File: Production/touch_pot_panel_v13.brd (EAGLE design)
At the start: 283 x 171.7 mm, 927 parts, among them U1 PIC16F1829, U10 5V, U11 PIC16F1829, U12 AD5262, U13 5V, U14 PIC16F1829, U15 AD5262, U16 5V, U17 PIC16F1829, U18 AD5262, U19 5V, U2 AD5262, U20 PIC16F1829, U21 AD5262, U22 5V, U23 PIC16F1829, U24 AD5262, U25 5V, U26 PIC16F1829, U27 AD5262, U28 5V, U29 PIC16F1829, U3 5V, U30 AD5262, U31 5V, U32 PIC16F1829, U33 AD5262, U34 5V, U35 PIC16F1829, U36 AD5262, U4 5V, U5 PIC16F1829, U6 AD5262, U7 5V, U8 PIC16F1829, U9 AD5262

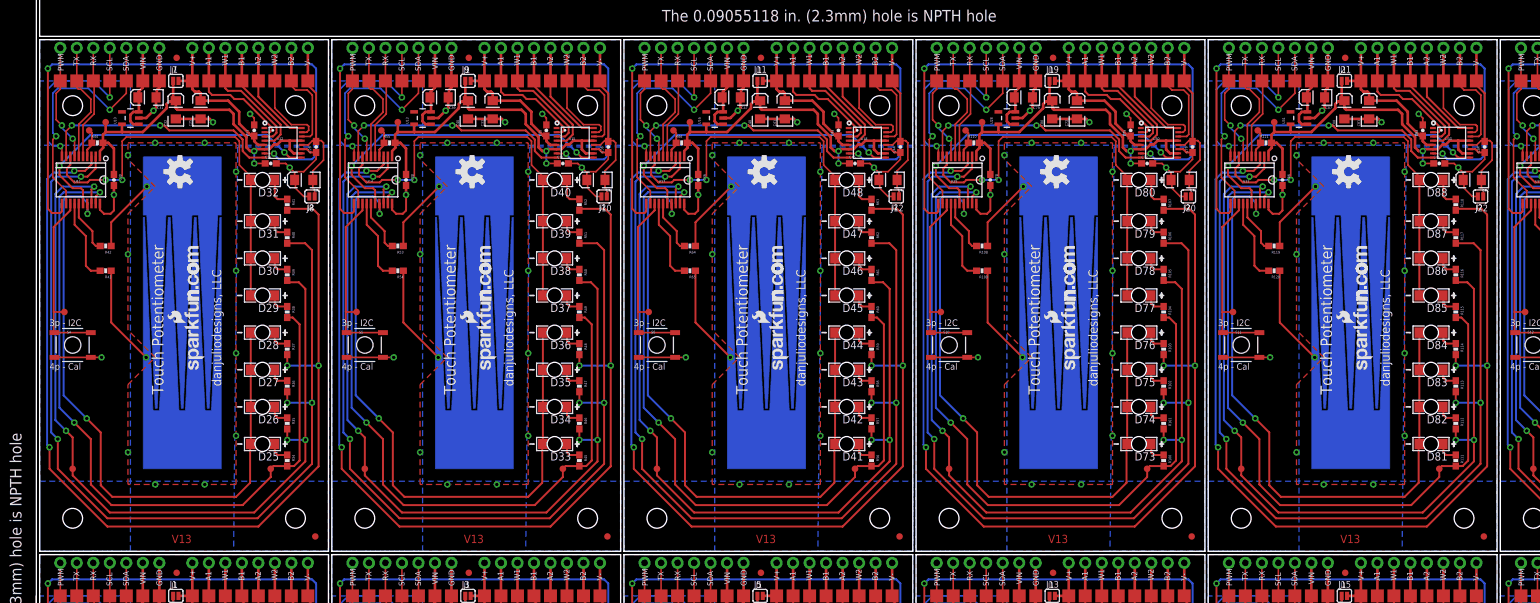
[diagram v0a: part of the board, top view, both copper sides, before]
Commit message: removed odd ground line
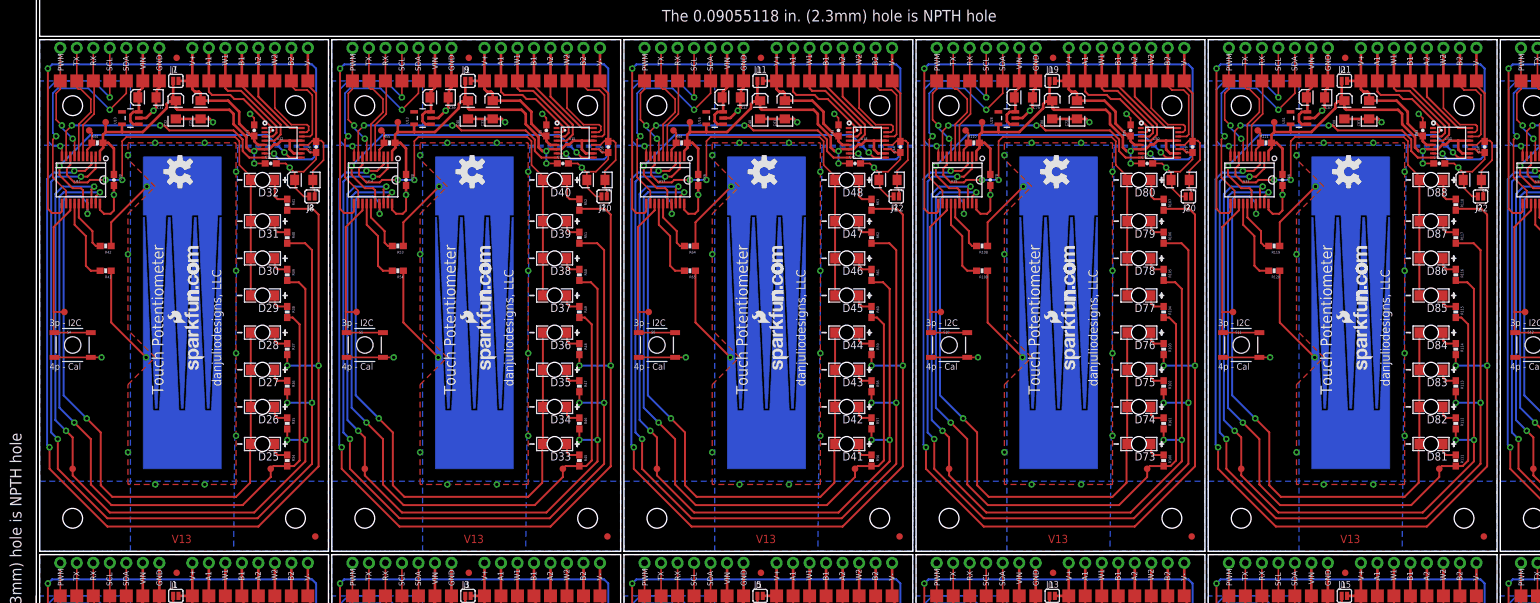
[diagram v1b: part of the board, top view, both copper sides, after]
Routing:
- net N$72: track 1.27 -> 0.00 mm
- net N$60: track 1.27 -> 0.00 mm
- net N$48: track 1.27 -> 0.00 mm
- net N$144: track 1.27 -> 0.00 mm
- net N$132: track 1.27 -> 0.00 mm
- net N$120: track 1.27 -> 0.00 mm
- net N$96: track 1.27 -> 0.00 mm
- net N$84: track 1.27 -> 0.00 mm
- net N$34: track 1.27 -> 0.00 mm
- net N$22: track 1.27 -> 0.00 mm
- net N$108: track 1.27 -> 0.00 mm
- net N$10: track 1.27 -> 0.00 mm
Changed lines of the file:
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@@
 <setting verticaltext="up"/>
 </settings>
-<grid distance="0.01" unitdist="inch" unit="inch" style="lines" multiple="1" display="yes" altdistance="0.001" altunitdist="inch" altunit="inch"/>
+<grid distance="0.05" unitdist="inch" unit="inch" style="lines" multiple="1" display="yes" altdistance="0.01" altunitdist="inch" altunit="inch"/>
 <layers>
 <layer number="1" name="Top" color="4" fill="1" visible="yes" active="yes"/>
@@
 <wire x1="14.478" y1="40.513" x2="9.398" y2="40.513" width="0.254" layer="1"/>
 </signal>
-<signal name="N$10">
-<wire x1="6.858" y1="84.328" x2="6.858" y2="85.598" width="0.2032" layer="16"/>
-</signal>
 <signal name="V+1">
 <contactref element="TP35" pad="P$1"/>
@@
 <wire x1="59.436" y1="40.513" x2="54.356" y2="40.513" width="0.254" layer="1"/>
 </signal>
-<signal name="N$22">
-<wire x1="51.816" y1="84.328" x2="51.816" y2="85.598" width="0.2032" layer="16"/>
-</signal>
 <signal name="V+2">
 <contactref element="TP55" pad="P$1"/>
@@
 <wire x1="104.394" y1="40.513" x2="99.314" y2="40.513" width="0.254" layer="1"/>
 </signal>
-<signal name="N$34">
-<wire x1="96.774" y1="84.328" x2="96.774" y2="85.598" width="0.2032" layer="16"/>
-</signal>
 <signal name="V+3">
 <contactref element="TP75" pad="P$1"/>
@@
 <wire x1="14.478" y1="119.761" x2="9.398" y2="119.761" width="0.254" layer="1"/>
 </signal>
-<signal name="N$48">
-<wire x1="6.858" y1="163.576" x2="6.858" y2="164.846" width="0.2032" layer="16"/>
-</signal>
 <signal name="V+4">
 <contactref element="TP95" pad="P$1"/>
@@
 <wire x1="59.436" y1="119.761" x2="54.356" y2="119.761" width="0.254" layer="1"/>
 </signal>
-<signal name="N$60">
-<wire x1="51.816" y1="163.576" x2="51.816" y2="164.846" width="0.2032" layer="16"/>
-</signal>
 <signal name="V+5">
 <contactref element="TP115" pad="P$1"/>
@@
 <wire x1="104.394" y1="119.761" x2="99.314" y2="119.761" width="0.254" layer="1"/>
 </signal>
-<signal name="N$72">
-<wire x1="96.774" y1="163.576" x2="96.774" y2="164.846" width="0.2032" layer="16"/>
-</signal>
 <signal name="V+6">
 <contactref element="TP135" pad="P$1"/>
@@
 <wire x1="149.352" y1="40.513" x2="144.272" y2="40.513" width="0.254" layer="1"/>
 </signal>
-<signal name="N$84">
-<wire x1="141.732" y1="84.328" x2="141.732" y2="85.598" width="0.2032" layer="16"/>
-</signal>
 <signal name="V+7">
 <contactref element="TP155" pad="P$1"/>
@@
 <wire x1="194.31" y1="40.513" x2="189.23" y2="40.513" width="0.254" layer="1"/>
 </signal>
-<signal name="N$96">
-<wire x1="186.69" y1="84.328" x2="186.69" y2="85.598" width="0.2032" layer="16"/>
-</signal>
 <signal name="V+8">
 <contactref element="TP175" pad="P$1"/>
@@
 <wire x1="239.268" y1="40.513" x2="234.188" y2="40.513" width="0.254" layer="1"/>
 </signal>
-<signal name="N$108">
-<wire x1="231.648" y1="84.328" x2="231.648" y2="85.598" width="0.2032" layer="16"/>
-</signal>
 <signal name="V+9">
 <contactref element="TP195" pad="P$1"/>
@@
 <wire x1="149.352" y1="119.761" x2="144.272" y2="119.761" width="0.254" layer="1"/>
 </signal>
-<signal name="N$120">
-<wire x1="141.732" y1="163.576" x2="141.732" y2="164.846" width="0.2032" layer="16"/>
-</signal>
 <signal name="V+10">
 <contactref element="TP215" pad="P$1"/>
@@
 <wire x1="194.31" y1="119.761" x2="189.23" y2="119.761" width="0.254" layer="1"/>
 </signal>
-<signal name="N$132">
-<wire x1="186.69" y1="163.576" x2="186.69" y2="164.846" width="0.2032" layer="16"/>
-</signal>
 <signal name="V+11">
 <contactref element="TP235" pad="P$1"/>
@@
 <wire x1="239.268" y1="119.761" x2="234.188" y2="119.761" width="0.254" layer="1"/>
 </signal>
-<signal name="N$144">
-<wire x1="231.648" y1="163.576" x2="231.648" y2="164.846" width="0.2032" layer="16"/>
-</signal>
 </signals>
